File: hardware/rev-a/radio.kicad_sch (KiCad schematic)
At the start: 10 parts, among them U4 SX1262, X3 32MHz

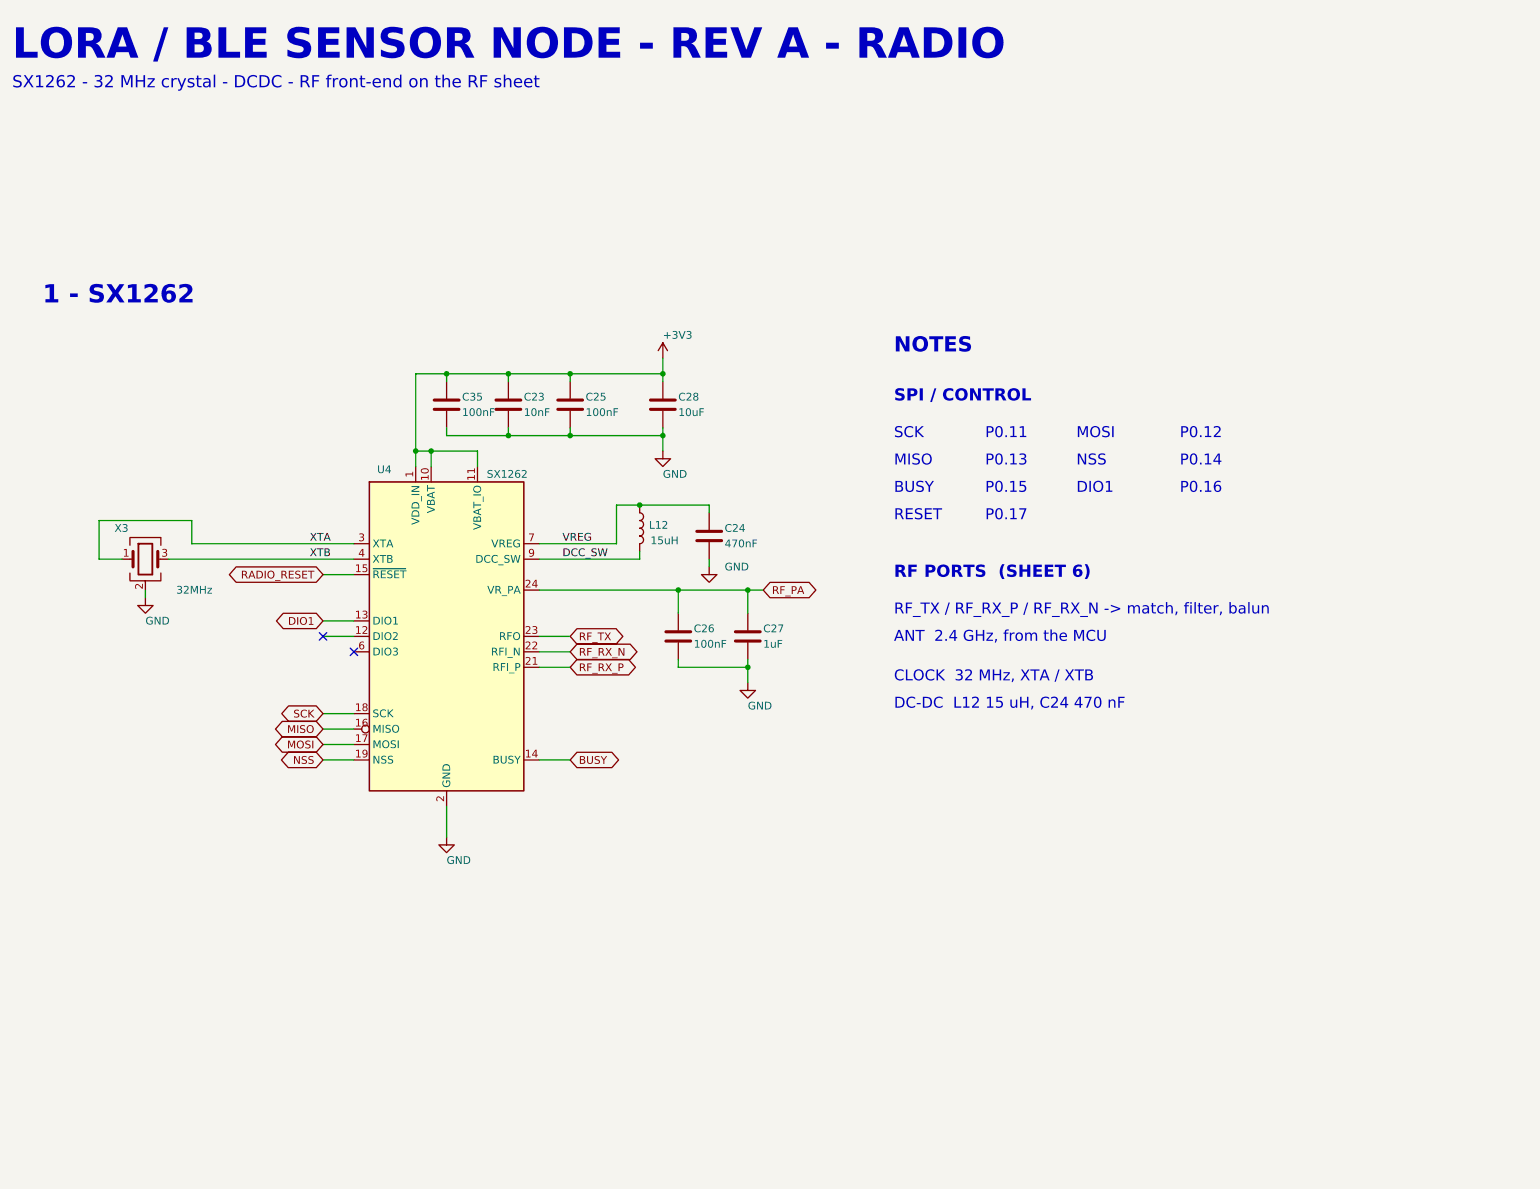
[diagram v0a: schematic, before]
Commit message: Schematic: cosmetic pass over the sheet artwork
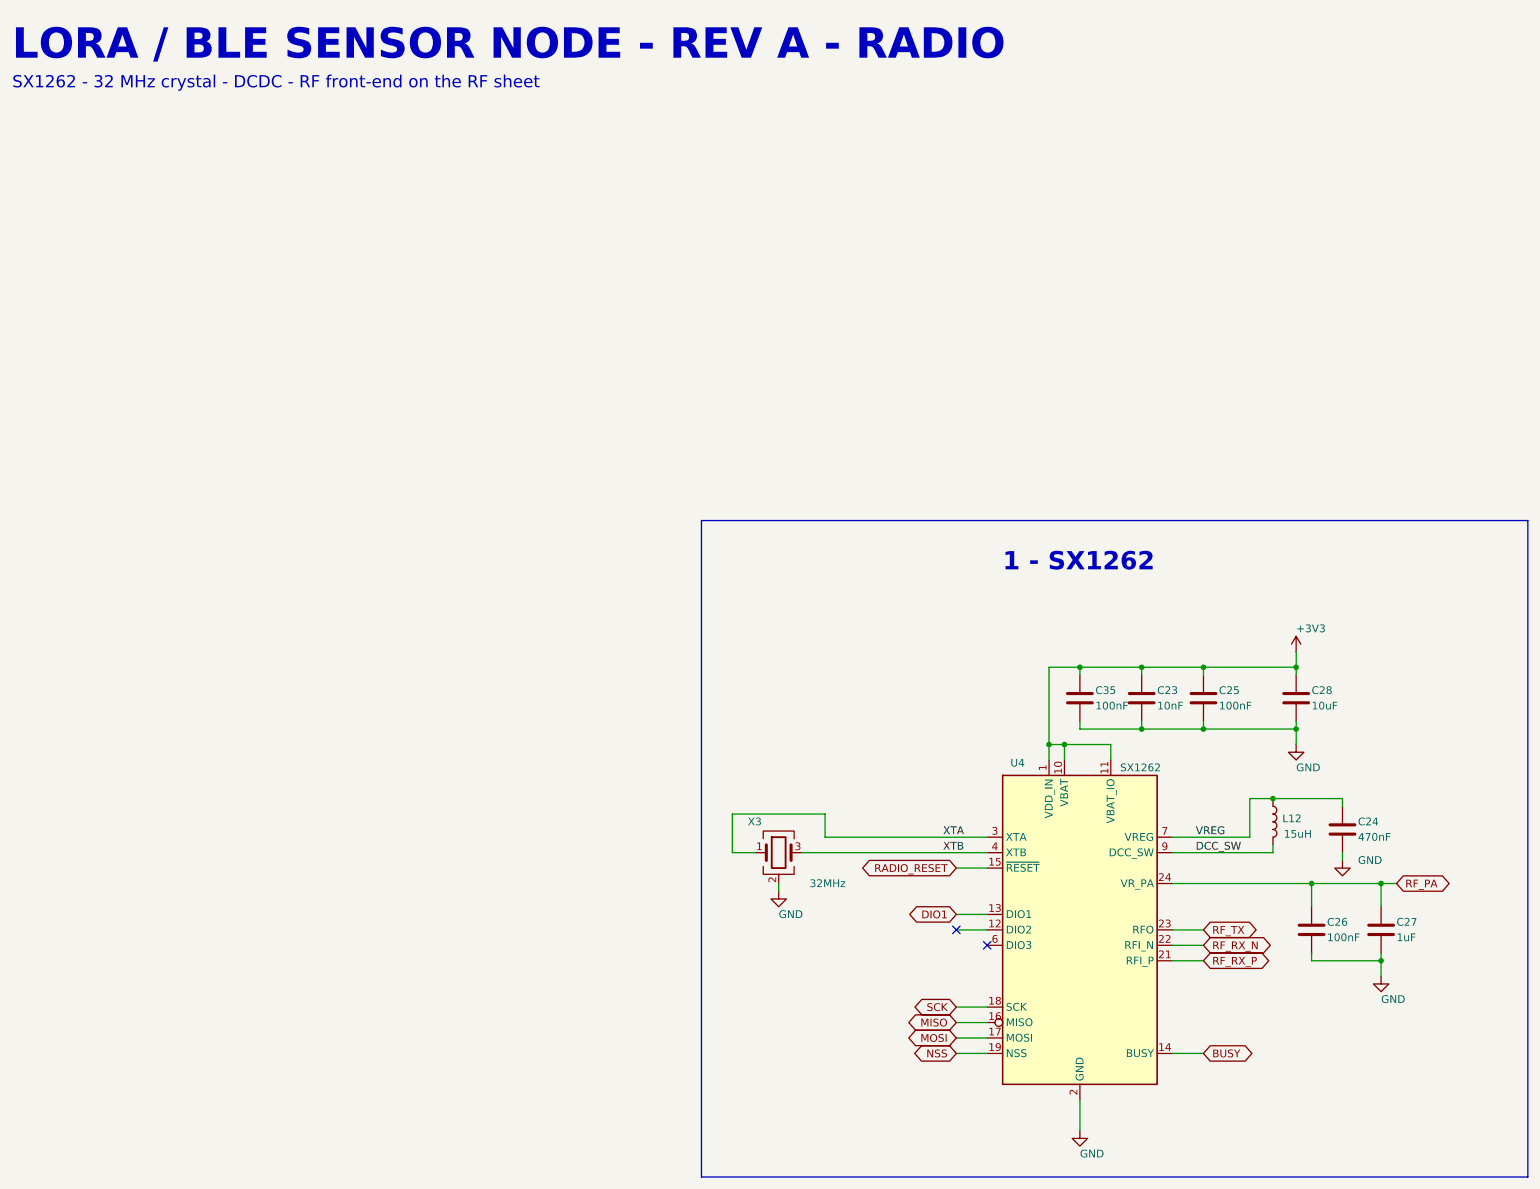
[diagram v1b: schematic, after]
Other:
- note removed: "ANT 2.4 GHz, from the MCU"
- note removed: "BUSY"
- note removed: "CLOCK 32 MHz, XTA / XTB"
- note removed: "DC-DC L12 15 uH, C24 470 nF"
- note removed: "DIO1"
- note removed: "MISO"
- note removed: "MOSI"
- note removed: "NOTES"
- note removed: "NSS"
- note removed: "P0.11"
- note removed: "P0.12"
- note removed: "P0.13"
- note removed: "P0.14"
- note removed: "P0.15"
- note removed: "P0.16"
- note removed: "P0.17"
- note removed: "RESET"
- note removed: "RF PORTS (SHEET 6)"
- note removed: "RF_TX / RF_RX_P / RF_RX_N -> match, filter, balun"
- note removed: "SCK"
- note removed: "SPI / CONTROL"
- moved on the sheet: C23, C24, C25, C26, C27, C28, C35, L12, U4, X3
